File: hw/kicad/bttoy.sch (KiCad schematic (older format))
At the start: 45 parts, among them J1 USB-micro-b, J2 HC-07_BLUETOOTH, J3 ARM_10PIN, P1 +9V, P10 M1+, P11 M1-, P12 M2+, P13 M2-, P14 B-, P15 B+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

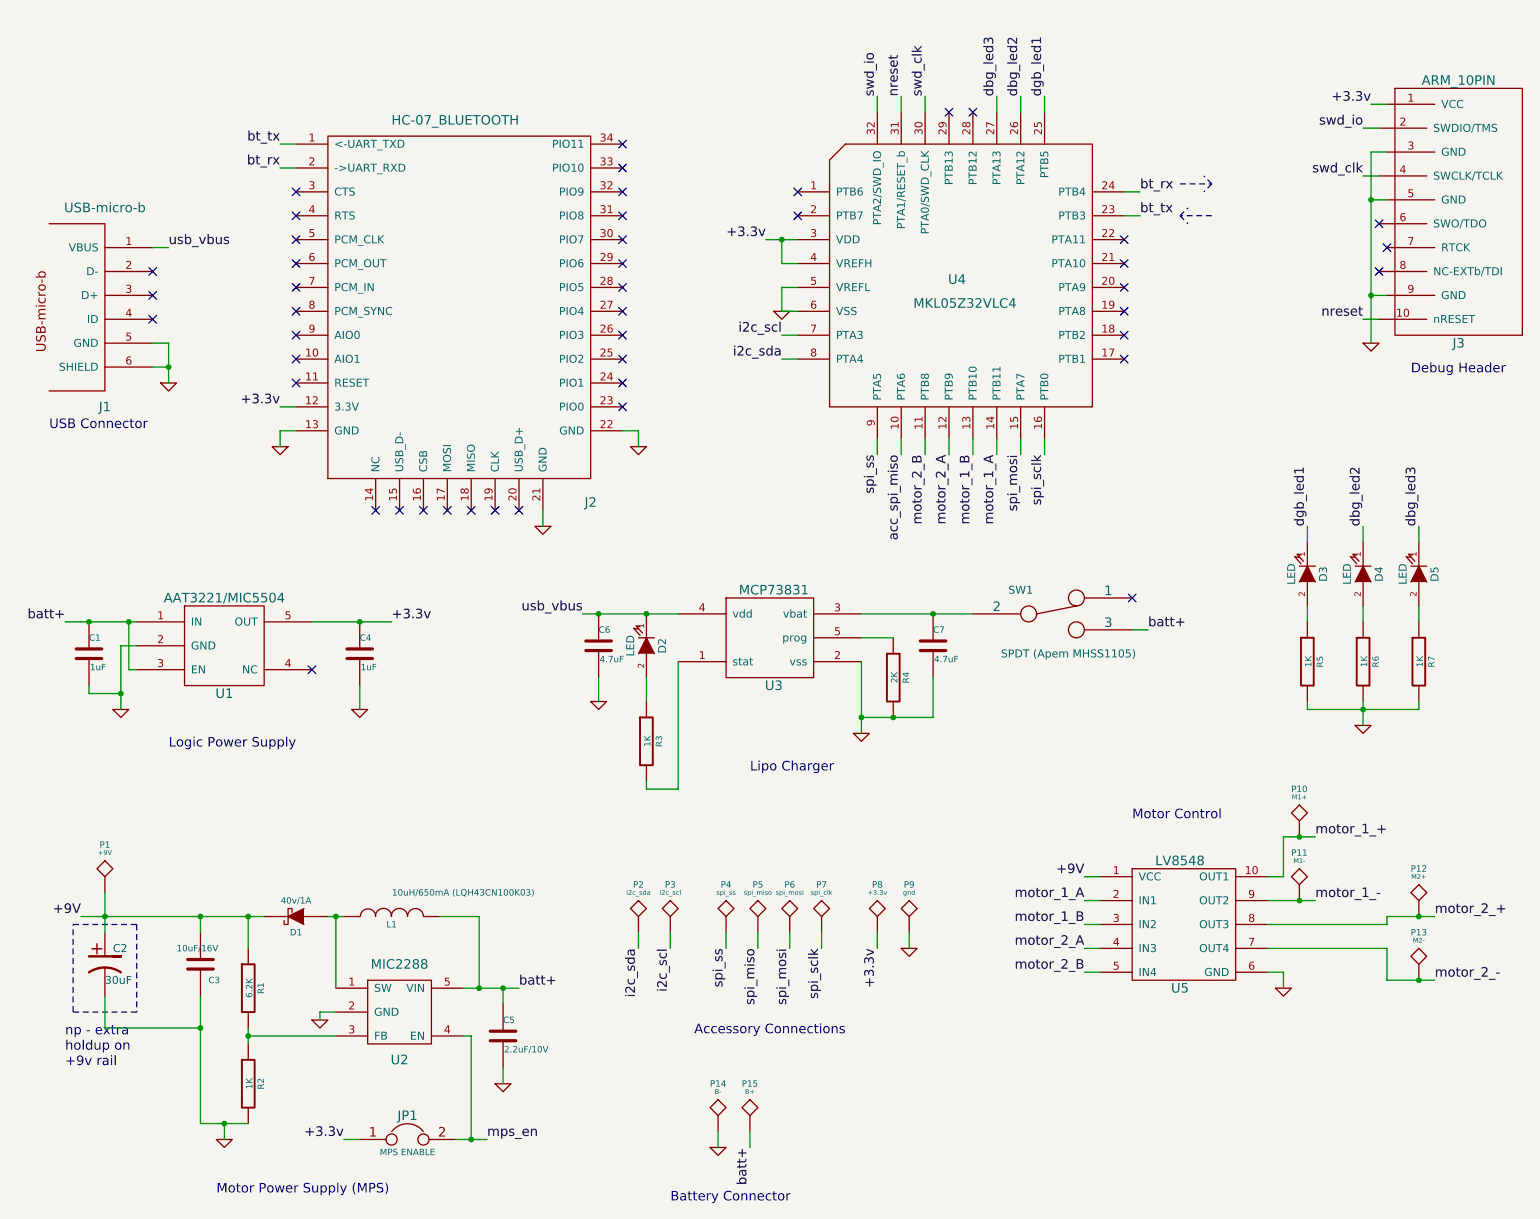
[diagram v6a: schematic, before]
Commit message: arrange footprint groups in pcb, change position of power switch to control all batt output
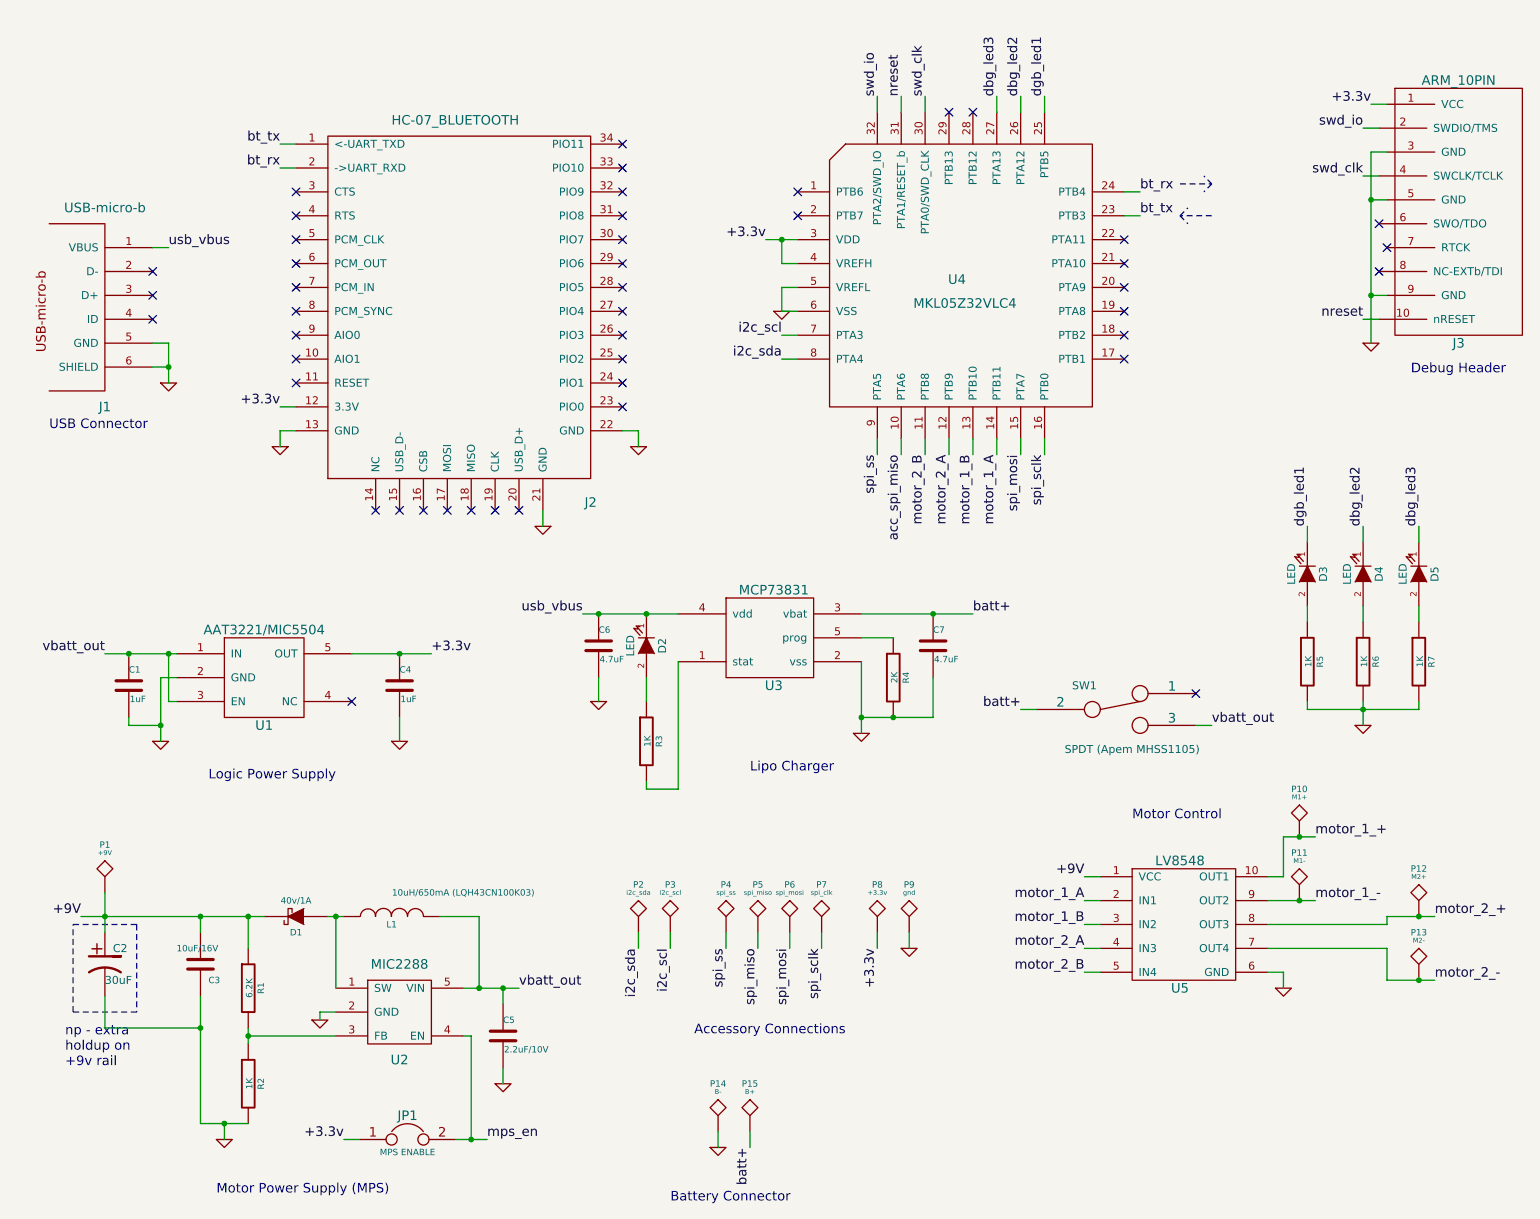
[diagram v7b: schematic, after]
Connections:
- net batt+: now also C7.1, SW1.2, U3.3 (vbat); no longer C1.1, C5.1, L1.2, SW1.3, U1.1 (IN), U1.3 (EN), U2.5 (VIN)
- new net vbatt_out: C1.1, C5.1, L1.2, SW1.3, U1.1 (IN), U1.3 (EN), U2.5 (VIN)
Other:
- moved on the sheet: C1, C4, SW1, U1
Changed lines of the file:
@@
 L AAT3221 U1
 U 1 1 5497812B
-P 1900 4450
-F 0 "U1" H 1900 4250 60  0000 C CNN
-F 1 "AAT3221/MIC5504" H 1900 4850 60  0000 C CNN
-F 2 "kicadlib:SMD_SOT23-5" H 1900 4450 60  0001 C CNN
-F 3 "" H 1900 4450 60  0000 C CNN
-	1    1900 4450
+P 2150 4650
+F 0 "U1" H 2150 4450 60  0000 C CNN
+F 1 "AAT3221/MIC5504" H 2150 5050 60  0000 C CNN
+F 2 "kicadlib:SMD_SOT23-5" H 2150 4650 60  0001 C CNN
+F 3 "" H 2150 4650 60  0000 C CNN
+	1    2150 4650
 	1    0    0    -1
 $EndComp
@@
 L C C1
 U 1 1 54EFD3D0
-P 1050 4400
-F 0 "C1" H 1050 4500 40  0000 L CNN
-F 1 "1uF" H 1056 4315 40  0000 L CNN
-F 2 "kicadlib:SMD_0603_R" H 1088 4250 30  0001 C CNN
-F 3 "" H 1050 4400 60  0000 C CNN
-	1    1050 4400
+P 1300 4600
+F 0 "C1" H 1300 4700 40  0000 L CNN
+F 1 "1uF" H 1306 4515 40  0000 L CNN
+F 2 "kicadlib:SMD_0603_R" H 1338 4450 30  0001 C CNN
+F 3 "" H 1300 4600 60  0000 C CNN
+	1    1300 4600
 	1    0    0    -1
 $EndComp
@@
 L C C4
 U 1 1 54EFD734
-P 2750 4400
-F 0 "C4" H 2750 4500 40  0000 L CNN
-F 1 "1uF" H 2756 4315 40  0000 L CNN
-F 2 "kicadlib:SMD_0603_R" H 2788 4250 30  0001 C CNN
-F 3 "" H 2750 4400 60  0000 C CNN
-	1    2750 4400
+P 3000 4600
+F 0 "C4" H 3000 4700 40  0000 L CNN
+F 1 "1uF" H 3006 4515 40  0000 L CNN
+F 2 "kicadlib:SMD_0603_R" H 3038 4450 30  0001 C CNN
+F 3 "" H 3000 4600 60  0000 C CNN
+	1    3000 4600
 	1    0    0    -1
 $EndComp
@@
 L GND #PWR04
 U 1 1 54EFD8F5
-P 1250 4750
-F 0 "#PWR04" H 1250 4750 30  0001 C CNN
-F 1 "GND" H 1250 4680 30  0001 C CNN
-F 2 "" H 1250 4750 60  0000 C CNN
-F 3 "" H 1250 4750 60  0000 C CNN
-	1    1250 4750
-	1    0    0    -1
-$EndComp
-NoConn ~ 2450 4500
-Text Label 900  4200 2    60   ~ 0
-batt+
-Text Label 2950 4200 0    60   ~ 0
+P 1500 4950
+F 0 "#PWR04" H 1500 4950 30  0001 C CNN
+F 1 "GND" H 1500 4880 30  0001 C CNN
+F 2 "" H 1500 4950 60  0000 C CNN
+F 3 "" H 1500 4950 60  0000 C CNN
+	1    1500 4950
+	1    0    0    -1
+$EndComp
+NoConn ~ 2700 4700
+Text Label 8100 4850 0    60   ~ 0
+vbatt_out
+Text Label 3200 4400 0    60   ~ 0
 +3.3v
 $Comp
 L GND #PWR05
 U 1 1 54EFDEE1
-P 2750 4750
-F 0 "#PWR05" H 2750 4750 30  0001 C CNN
-F 1 "GND" H 2750 4680 30  0001 C CNN
-F 2 "" H 2750 4750 60  0000 C CNN
-F 3 "" H 2750 4750 60  0000 C CNN
-	1    2750 4750
+P 3000 4950
+F 0 "#PWR05" H 3000 4950 30  0001 C CNN
+F 1 "GND" H 3000 4880 30  0001 C CNN
+F 2 "" H 3000 4950 60  0000 C CNN
+F 3 "" H 3000 4950 60  0000 C CNN
+	1    3000 4950
 	1    0    0    -1
 $EndComp
@@
 Text Notes 5200 5150 0    60   ~ 0
 Lipo Charger
-Text Notes 1550 5000 0    60   ~ 0
+Text Notes 1800 5200 0    60   ~ 0
 Logic Power Supply
 Text Notes 9350 2650 0    60   ~ 0
@@
 	0    -1   -1   0
 $EndComp
-Text Label 3750 6500 0    60   ~ 0
-batt+
 $Comp
 L C C5
@@
 L SWITCH_INV SW1
 U 1 1 54F51E0E
-P 7100 4150
-F 0 "SW1" H 6900 4300 50  0000 C CNN
-F 1 "SPDT (Apem MHSS1105)" H 7200 3900 50  0000 C CNN
-F 2 "kicadlib:TH_APEM_MHSS1105_SPDT" H 7100 4150 60  0001 C CNN
-F 3 "" H 7100 4150 60  0000 C CNN
-	1    7100 4150
-	1    0    0    -1
-$EndComp
-Text Label 7700 4250 0    60   ~ 0
+P 7500 4750
+F 0 "SW1" H 7300 4900 50  0000 C CNN
+F 1 "SPDT (Apem MHSS1105)" H 7600 4500 50  0000 C CNN
+F 2 "kicadlib:TH_APEM_MHSS1105_SPDT" H 7500 4750 60  0001 C CNN
+F 3 "" H 7500 4750 60  0000 C CNN
+	1    7500 4750
+	1    0    0    -1
+$EndComp
+Text Label 6600 4150 0    60   ~ 0
 batt+
-NoConn ~ 7600 4050
+NoConn ~ 8000 4650
 Text Label 3550 7450 0    60   ~ 0
 mps_en
@@
 Connection ~ 1550 2600
 Wire Wire Line
-	2450 4200 2950 4200
-Wire Wire Line
-	900  4200 1350 4200
-Wire Wire Line
-	1250 4350 1250 4750
-Wire Wire Line
-	1250 4350 1350 4350
-Wire Wire Line
-	1050 4600 1050 4650
-Wire Wire Line
-	1050 4650 1250 4650
-Connection ~ 1250 4650
-Wire Wire Line
-	1350 4500 1300 4500
-Wire Wire Line
-	1300 4500 1300 4200
-Connection ~ 1300 4200
+	2700 4400 3200 4400
+Wire Wire Line
+	1150 4400 1600 4400
+Wire Wire Line
+	1500 4550 1500 4950
+Wire Wire Line
+	1500 4550 1600 4550
+Wire Wire Line
+	1300 4800 1300 4850
+Wire Wire Line
+	1300 4850 1500 4850
+Connection ~ 1500 4850
+Wire Wire Line
+	1600 4700 1550 4700
+Wire Wire Line
+	1550 4700 1550 4400
+Connection ~ 1550 4400
 Connection ~ 6350 4150
-Connection ~ 1050 4200
-Connection ~ 2750 4200
-Wire Wire Line
-	2750 4750 2750 4600
+Connection ~ 1300 4400
+Connection ~ 3000 4400
+Wire Wire Line
+	3000 4950 3000 4800
 Wire Wire Line
 	5400 2250 5500 2250
@@
 Wire Wire Line
 	3450 6800 3400 6800
-Wire Wire Line
-	7700 4250 7600 4250
 Connection ~ 3450 7450
 Connection ~ 1750 6050
@@
 NoConn ~ 7550 2400
 NoConn ~ 7550 2550
+Text Label 6900 4750 2    60   ~ 0
+batt+
+Wire Wire Line
+	6900 4750 7000 4750
+Wire Wire Line
+	8100 4850 8000 4850
+Text Label 1150 4400 2    60   ~ 0
+vbatt_out
+Text Label 3750 6500 0    60   ~ 0
+vbatt_out
 $EndSCHEMATC

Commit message: place test points
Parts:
- added P16: gnd, kicadlib:TEST_0.100, symbol TST
- C1, C3, C4, C5, C6, C7: symbol C -> C-RESCUE-bttoy
- C2: symbol CP1 -> CP1-RESCUE-bttoy
- P1: value +9V -> gnd
- R1, R2, R3, R4, R5, R6, R7: symbol R -> R-RESCUE-bttoy
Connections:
- net +9V: no longer P1.1
- net GND: now also P1.1, P16.1
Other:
- moved on the sheet: P4, P5, P6, P7, P8, P9
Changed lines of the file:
@@
 EESchema Schematic File Version 2
+LIBS:bttoy-rescue
 LIBS:power
 LIBS:device
@@
 LIBS:memory
 LIBS:xilinx
-LIBS:special
 LIBS:microcontrollers
 LIBS:dsp
@@
 motor_2_B
 $Comp
-L R R3
+L R-RESCUE-bttoy R3
 U 1 1 54EFC2B0
 P 4550 4950
@@
 $EndComp
 $Comp
-L C C6
+L C-RESCUE-bttoy C6
 U 1 1 54EFC2D7
 P 4250 4350
@@
 $EndComp
 $Comp
-L R R4
+L R-RESCUE-bttoy R4
 U 1 1 54EFC5FD
 P 6100 4550
@@
 $EndComp
 $Comp
-L C C7
+L C-RESCUE-bttoy C7
 U 1 1 54EFC66F
 P 6350 4350
@@
 $EndComp
 $Comp
-L GND #PWR01
+L GND-RESCUE-bttoy #PWR01
 U 1 1 54EFC814
 P 4250 4700
@@
 $EndComp
 $Comp
-L GND #PWR02
+L GND-RESCUE-bttoy #PWR02
 U 1 1 54EFC8B1
 P 5900 4900
@@
 NoConn ~ 1450 2300
 $Comp
-L GND #PWR03
+L GND-RESCUE-bttoy #PWR03
 U 1 1 54EFD0DA
 P 1550 2700
@@
 $EndComp
 $Comp
-L C C1
+L C-RESCUE-bttoy C1
 U 1 1 54EFD3D0
 P 1300 4600
@@
 $EndComp
 $Comp
-L C C4
+L C-RESCUE-bttoy C4
 U 1 1 54EFD734
 P 3000 4600
@@
 $EndComp
 $Comp
-L GND #PWR04
+L GND-RESCUE-bttoy #PWR04
 U 1 1 54EFD8F5
 P 1500 4950
@@
 +3.3v
 $Comp
-L GND #PWR05
+L GND-RESCUE-bttoy #PWR05
 U 1 1 54EFDEE1
 P 3000 4950
@@
 $EndComp
 $Comp
-L GND #PWR06
+L GND-RESCUE-bttoy #PWR06
 U 1 1 54EFE071
 P 5400 2250
@@
 $EndComp
 $Comp
-L GND #PWR07
+L GND-RESCUE-bttoy #PWR07
 U 1 1 54EFE527
 P 9100 2450
@@
 $EndComp
 $Comp
-L C C5
+L C-RESCUE-bttoy C5
 U 1 1 54F4F2D9
 P 3650 6800
@@
 $EndComp
 $Comp
-L GND #PWR08
+L GND-RESCUE-bttoy #PWR08
 U 1 1 54F4F4A4
 P 3650 7100
@@
 $EndComp
 $Comp
-L C C3
+L C-RESCUE-bttoy C3
 U 1 1 54F4F68E
 P 1750 6350
@@
 $EndComp
 $Comp
-L GND #PWR09
+L GND-RESCUE-bttoy #PWR09
 U 1 1 54F4F9FC
 P 1900 7450
@@
 $EndComp
 $Comp
-L R R1
+L R-RESCUE-bttoy R1
 U 1 1 54F4FB8E
 P 2050 6500
@@
 $EndComp
 $Comp
-L R R2
+L R-RESCUE-bttoy R2
 U 1 1 54F5000A
 P 2050 7100
@@
 $EndComp
 $Comp
-L GND #PWR010
+L GND-RESCUE-bttoy #PWR010
 U 1 1 54F506B9
 P 2500 6700
@@
 +3.3v
 $Comp
-L GND #PWR011
+L GND-RESCUE-bttoy #PWR011
 U 1 1 54F52E71
 P 2250 3100
@@
 +9V
 $Comp
-L CP1 C2
+L CP1-RESCUE-bttoy C2
 U 1 1 54F55200
 P 1150 6350
@@
 $EndComp
 $Comp
-L GND #PWR012
+L GND-RESCUE-bttoy #PWR012
 U 1 1 54FC64F5
 P 8550 6500
@@
 	1    0    0    -1
 $EndComp
-$Comp
-L TST P1
-U 1 1 54FCC050
-P 1150 5900
-F 0 "P1" H 1150 6200 40  0000 C CNN
-F 1 "+9V" H 1150 6150 30  0000 C CNN
-F 2 "kicadlib:TEST_0.100" H 1150 5900 60  0001 C CNN
-F 3 "" H 1150 5900 60  0000 C CNN
-	1    1150 5900
-	1    0    0    -1
-$EndComp
 Wire Wire Line
 	4750 4450 4750 5250
@@
 Connection ~ 3450 7450
 Connection ~ 1750 6050
-Wire Wire Line
-	1150 5900 1150 6150
-Connection ~ 1150 6050
 Wire Wire Line
 	1150 6550 1150 6750
@@
 	2250 3000 2250 3100
 $Comp
-L GND #PWR013
+L GND-RESCUE-bttoy #PWR013
 U 1 1 55044EE6
 P 3900 3600
@@
 $EndComp
 $Comp
-L GND #PWR014
+L GND-RESCUE-bttoy #PWR014
 U 1 1 55044F0E
 P 4500 3100
@@
 $EndComp
 $Comp
-L R R5
+L R-RESCUE-bttoy R5
 U 1 1 5504817F
 P 8700 4450
@@
 $EndComp
 $Comp
-L R R6
+L R-RESCUE-bttoy R6
 U 1 1 550484FA
 P 9050 4450
@@
 $EndComp
 $Comp
-L R R7
+L R-RESCUE-bttoy R7
 U 1 1 55048593
 P 9400 4450
@@
 	9400 4100 9400 4200
 $Comp
-L GND #PWR015
+L GND-RESCUE-bttoy #PWR015
 U 1 1 55048626
 P 9050 4850
@@
 L TST P6
 U 1 1 55327637
-P 5450 6150
-F 0 "P6" H 5450 6450 40  0000 C CNN
-F 1 "spi_mosi" H 5450 6400 30  0000 C CNN
-F 2 "kicadlib:TEST_0.100" H 5450 6150 60  0001 C CNN
-F 3 "" H 5450 6150 60  0000 C CNN
-	1    5450 6150
+P 5600 6150
+F 0 "P6" H 5600 6450 40  0000 C CNN
+F 1 "spi_mosi" H 5600 6400 30  0000 C CNN
+F 2 "kicadlib:TEST_0.100" H 5600 6150 60  0001 C CNN
+F 3 "" H 5600 6150 60  0000 C CNN
+	1    5600 6150
 	1    0    0    -1
 $EndComp
@@
 L TST P5
 U 1 1 55327834
-P 5250 6150
-F 0 "P5" H 5250 6450 40  0000 C CNN
-F 1 "spi_miso" H 5250 6400 30  0000 C CNN
-F 2 "kicadlib:TEST_0.100" H 5250 6150 60  0001 C CNN
-F 3 "" H 5250 6150 60  0000 C CNN
-	1    5250 6150
+P 5400 6150
+F 0 "P5" H 5400 6450 40  0000 C CNN
+F 1 "spi_miso" H 5400 6400 30  0000 C CNN
+F 2 "kicadlib:TEST_0.100" H 5400 6150 60  0001 C CNN
+F 3 "" H 5400 6150 60  0000 C CNN
+	1    5400 6150
 	1    0    0    -1
 $EndComp
@@
 L TST P4
 U 1 1 553278C8
-P 5050 6150
-F 0 "P4" H 5050 6450 40  0000 C CNN
-F 1 "spi_ss" H 5050 6400 30  0000 C CNN
-F 2 "kicadlib:TEST_0.100" H 5050 6150 60  0001 C CNN
-F 3 "" H 5050 6150 60  0000 C CNN
-	1    5050 6150
+P 5200 6150
+F 0 "P4" H 5200 6450 40  0000 C CNN
+F 1 "spi_ss" H 5200 6400 30  0000 C CNN
+F 2 "kicadlib:TEST_0.100" H 5200 6150 60  0001 C CNN
+F 3 "" H 5200 6150 60  0000 C CNN
+	1    5200 6150
 	1    0    0    -1
 $EndComp
@@
 L TST P7
 U 1 1 55327965
-P 5650 6150
-F 0 "P7" H 5650 6450 40  0000 C CNN
-F 1 "spi_clk" H 5650 6400 30  0000 C CNN
-F 2 "kicadlib:TEST_0.100" H 5650 6150 60  0001 C CNN
-F 3 "" H 5650 6150 60  0000 C CNN
-	1    5650 6150
+P 5800 6150
+F 0 "P7" H 5800 6450 40  0000 C CNN
+F 1 "spi_clk" H 5800 6400 30  0000 C CNN
+F 2 "kicadlib:TEST_0.100" H 5800 6150 60  0001 C CNN
+F 3 "" H 5800 6150 60  0000 C CNN
+	1    5800 6150
 	1    0    0    -1
 $EndComp
@@
 Wire Wire Line
 	4700 6150 4700 6250
-Text Label 5250 6250 3    60   ~ 0
+Text Label 5400 6250 3    60   ~ 0
 spi_miso
-Text Label 5050 6250 3    60   ~ 0
+Text Label 5200 6250 3    60   ~ 0
 spi_ss
-Text Label 5450 6250 3    60   ~ 0
+Text Label 5600 6250 3    60   ~ 0
 spi_mosi
-Text Label 5650 6250 3    60   ~ 0
+Text Label 5800 6250 3    60   ~ 0
 spi_sclk
 Wire Wire Line
-	5050 6250 5050 6150
-Wire Wire Line
-	5250 6150 5250 6250
-Wire Wire Line
-	5450 6250 5450 6150
-Wire Wire Line
-	5650 6150 5650 6250
+	5200 6250 5200 6150
+Wire Wire Line
+	5400 6150 5400 6250
+Wire Wire Line
+	5600 6250 5600 6150
+Wire Wire Line
+	5800 6150 5800 6250
 $Comp
 L TST P8
 U 1 1 55329B57
-P 6000 6150
-F 0 "P8" H 6000 6450 40  0000 C CNN
-F 1 "+3.3v" H 6000 6400 30  0000 C CNN
-F 2 "kicadlib:TEST_0.100" H 6000 6150 60  0001 C CNN
-F 3 "" H 6000 6150 60  0000 C CNN
-	1    6000 6150
+P 6250 6150
+F 0 "P8" H 6250 6450 40  0000 C CNN
+F 1 "+3.3v" H 6250 6400 30  0000 C CNN
+F 2 "kicadlib:TEST_0.100" H 6250 6150 60  0001 C CNN
+F 3 "" H 6250 6150 60  0000 C CNN
+	1    6250 6150
 	1    0    0    -1
 $EndComp
@@
 L TST P9
 U 1 1 55329C7E
-P 6200 6150
-F 0 "P9" H 6200 6450 40  0000 C CNN
-F 1 "gnd" H 6200 6400 30  0000 C CNN
-F 2 "kicadlib:TEST_0.100" H 6200 6150 60  0001 C CNN
-F 3 "" H 6200 6150 60  0000 C CNN
-	1    6200 6150
-	1    0    0    -1
-$EndComp
-Text Label 6000 6250 3    60   ~ 0
+P 6450 6150
+F 0 "P9" H 6450 6450 40  0000 C CNN
+F 1 "gnd" H 6450 6400 30  0000 C CNN
+F 2 "kicadlib:TEST_0.100" H 6450 6150 60  0001 C CNN
+F 3 "" H 6450 6150 60  0000 C CNN
+	1    6450 6150
+	1    0    0    -1
+$EndComp
+Text Label 6250 6250 3    60   ~ 0
 +3.3v
 $Comp
-L GND #PWR016
+L GND-RESCUE-bttoy #PWR016
 U 1 1 5532A219
-P 6200 6250
-F 0 "#PWR016" H 6200 6250 30  0001 C CNN
-F 1 "GND" H 6200 6180 30  0001 C CNN
-F 2 "" H 6200 6250 60  0000 C CNN
-F 3 "" H 6200 6250 60  0000 C CNN
-	1    6200 6250
-	1    0    0    -1
-$EndComp
-Wire Wire Line
-	6200 6250 6200 6150
-Wire Wire Line
-	6000 6150 6000 6250
+P 6450 6250
+F 0 "#PWR016" H 6450 6250 30  0001 C CNN
+F 1 "GND" H 6450 6180 30  0001 C CNN
+F 2 "" H 6450 6250 60  0000 C CNN
+F 3 "" H 6450 6250 60  0000 C CNN
+	1    6450 6250
+	1    0    0    -1
+$EndComp
+Wire Wire Line
+	6450 6250 6450 6150
+Wire Wire Line
+	6250 6150 6250 6250
 Text Notes 4850 6800 0    60   ~ 0
 Accessory Connections
@@
 batt+
 $Comp
-L GND #PWR017
+L GND-RESCUE-bttoy #PWR017
 U 1 1 5536D437
 P 5000 7500
@@
 Text Label 3750 6500 0    60   ~ 0
 vbatt_out
+Wire Wire Line
+	1150 6150 1150 6050
+Connection ~ 1150 6050
+$Comp
+L TST P1
+U 1 1 55F6C22E
+P 4900 6150
+F 0 "P1" H 4900 6450 40  0000 C CNN
+F 1 "gnd" H 4900 6400 30  0000 C CNN
+F 2 "kicadlib:TEST_0.100" H 4900 6150 60  0001 C CNN
+F 3 "" H 4900 6150 60  0000 C CNN
+	1    4900 6150
+	1    0    0    -1
+$EndComp
+$Comp
+L TST P16
+U 1 1 55F6C2D8
+P 6000 6150
+F 0 "P16" H 6000 6450 40  0000 C CNN
+F 1 "gnd" H 6000 6400 30  0000 C CNN
+F 2 "kicadlib:TEST_0.100" H 6000 6150 60  0001 C CNN
+F 3 "" H 6000 6150 60  0000 C CNN
+	1    6000 6150
+	1    0    0    -1
+$EndComp
+$Comp
+L GND-RESCUE-bttoy #PWR018
+U 1 1 55F6C360
+P 4900 6250
+F 0 "#PWR018" H 4900 6250 30  0001 C CNN
+F 1 "GND" H 4900 6180 30  0001 C CNN
+F 2 "" H 4900 6250 60  0000 C CNN
+F 3 "" H 4900 6250 60  0000 C CNN
+	1    4900 6250
+	1    0    0    -1
+$EndComp
+$Comp
+L GND-RESCUE-bttoy #PWR019
+U 1 1 55F6C3C7
+P 6000 6250
+F 0 "#PWR019" H 6000 6250 30  0001 C CNN
+F 1 "GND" H 6000 6180 30  0001 C CNN
+F 2 "" H 6000 6250 60  0000 C CNN
+F 3 "" H 6000 6250 60  0000 C CNN
+	1    6000 6250
+	1    0    0    -1
+$EndComp
+Wire Wire Line
+	6000 6250 6000 6150
+Wire Wire Line
+	4900 6250 4900 6150
 $EndSCHEMATC
